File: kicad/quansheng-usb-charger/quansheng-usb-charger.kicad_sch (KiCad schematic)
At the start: 32 parts, among them J1 USB_C_Receptacle_USB2.0, U1 IP2326

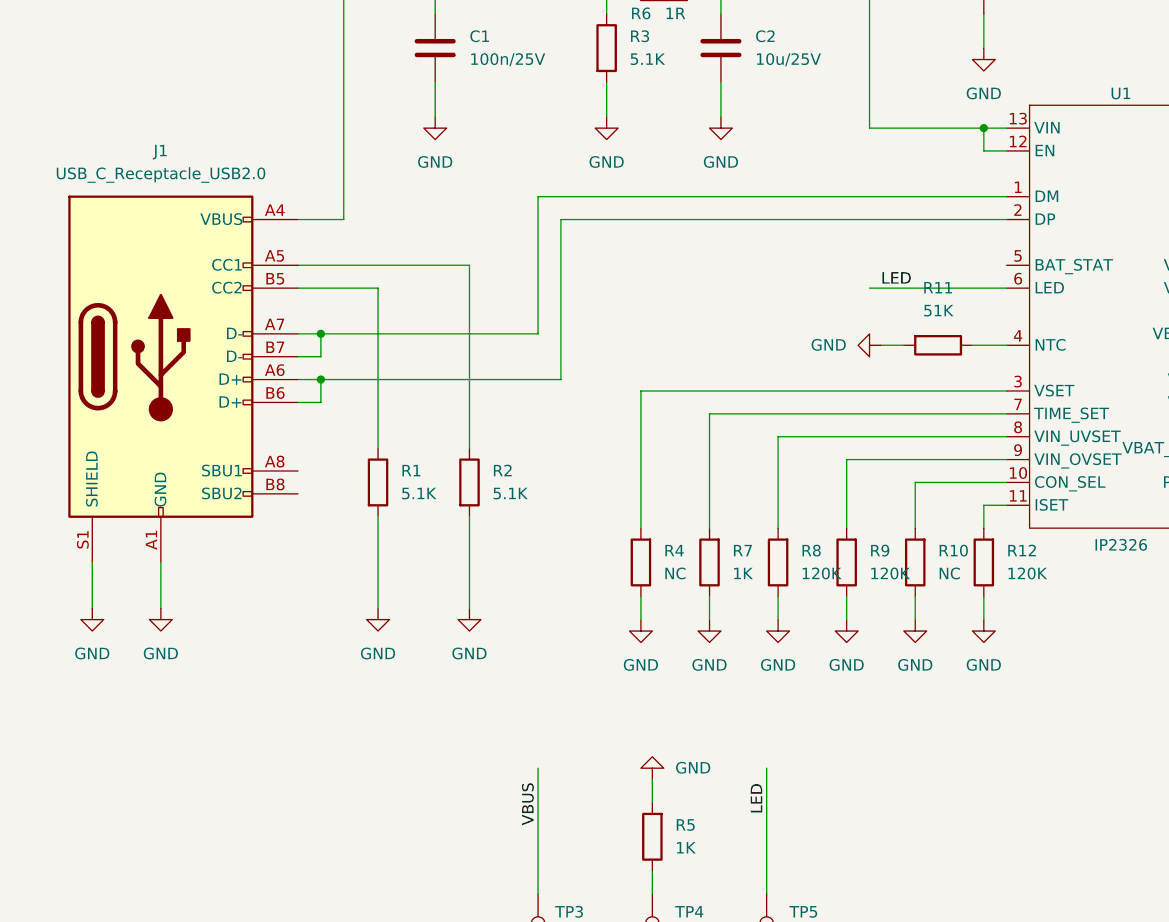
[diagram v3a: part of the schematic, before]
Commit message: Don't use the built-in USB AFC standard
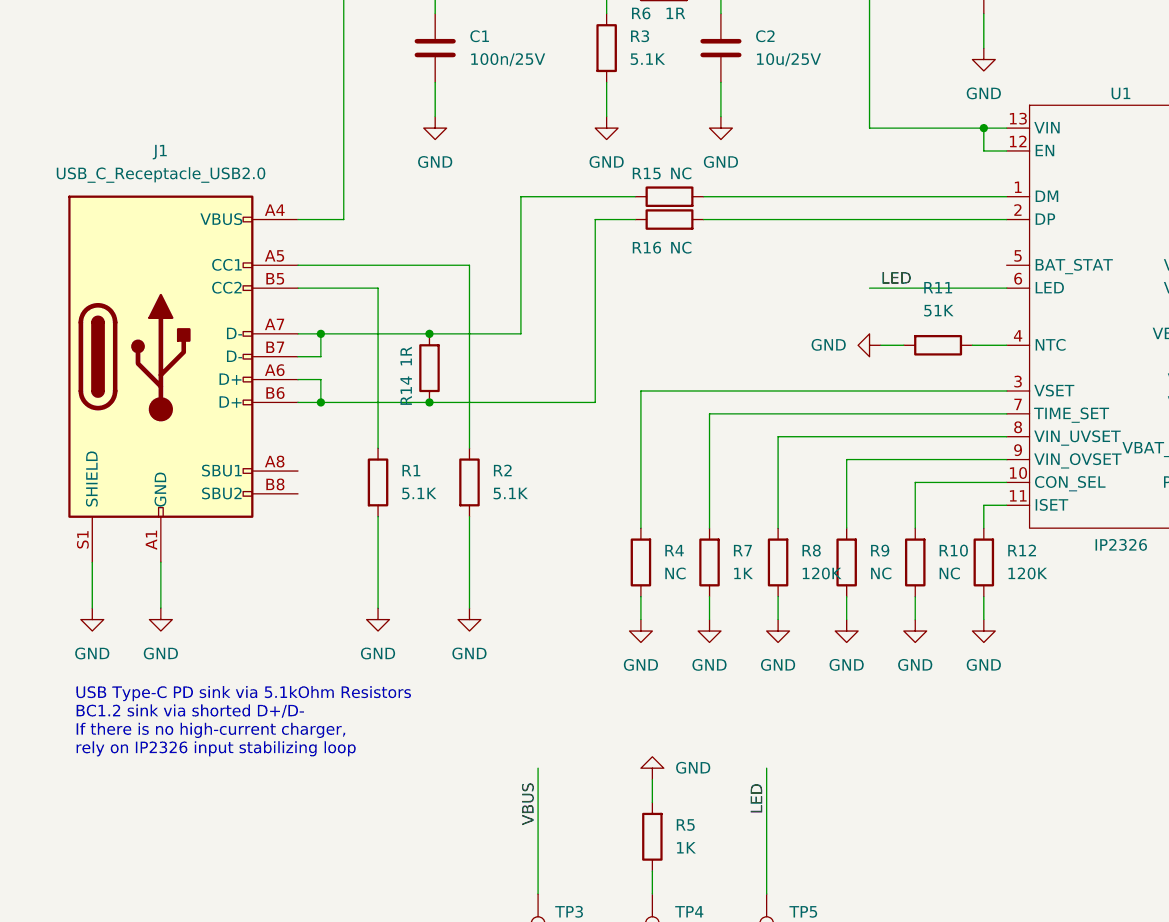
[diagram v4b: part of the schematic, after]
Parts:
- added R14: 1R, Resistor_SMD:R_0603_1608Metric, symbol Device:R
- added R15, R16: NC, Resistor_SMD:R_0603_1608Metric, symbol Device:R
- R9: value 120K -> NC; LCSC C25808 -> (none)
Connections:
- net at J1.A6 (D+), J1.B6 (D+): now also R14.1, R16.1; no longer U1.2 (DP)
- net at J1.A7 (D-), J1.B7 (D-): now also R14.2, R15.1; no longer U1.1 (DM)
- new net: R15.2, U1.1 (DM)
- new net: R16.2, U1.2 (DP)
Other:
- note added: "USB Type-C PD sink via 5.1kOhm Resistors BC1.2 sink via shorted D+/D- If there is no high-current charger, rely on IP2326 input stabilizing loop"
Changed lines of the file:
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@@
   (junction (at 177.8 99.06) (diameter 0) (color 0 0 0 0)
   )
+  (junction (at 75.565 99.06) (diameter 0) (color 0 0 0 0)
+  )
   (junction (at 171.45 68.58) (diameter 0) (color 0 0 0 0)
   )
@@
   (junction (at 107.95 53.34) (diameter 0) (color 0 0 0 0)
   )
+  (junction (at 63.5 99.06) (diameter 0) (color 0 0 0 0)
+  )
   (junction (at 95.25 53.34) (diameter 0) (color 0 0 0 0)
   )
-  (junction (at 63.5 96.52) (diameter 0) (color 0 0 0 0)
-  )
   (junction (at 137.16 44.45) (diameter 0) (color 0 0 0 0)
   )
@@
   (junction (at 95.25 50.165) (diameter 0) (color 0 0 0 0)
   )
+  (junction (at 75.565 91.44) (diameter 0) (color 0 0 0 0)
+  )
   (junction (at 95.25 44.45) (diameter 0) (color 0 0 0 0)
   )
@@
     (stroke (width 0) (type default) (color 0 0 0 0))
   )
+  (wire (pts (xy 75.565 99.06) (xy 93.98 99.06))
+    (stroke (width 0) (type default) (color 0 0 0 0))
+  )
+  (wire (pts (xy 98.425 78.74) (xy 93.98 78.74))
+    (stroke (width 0) (type default) (color 0 0 0 0))
+  )
   (wire (pts (xy 125.73 92.71) (xy 128.27 92.71))
     (stroke (width 0) (type default) (color 0 0 0 0))
@@
     (stroke (width 0) (type default) (color 0 0 0 0))
   )
-  (wire (pts (xy 63.5 91.44) (xy 87.63 91.44))
+  (wire (pts (xy 63.5 91.44) (xy 75.565 91.44))
     (stroke (width 0) (type default) (color 0 0 0 0))
   )
@@
     (stroke (width 0) (type default) (color 0 0 0 0))
   )
-  (wire (pts (xy 90.17 96.52) (xy 63.5 96.52))
+  (wire (pts (xy 106.045 76.2) (xy 139.7 76.2))
+    (stroke (width 0) (type default) (color 0 0 0 0))
+  )
+  (wire (pts (xy 93.98 78.74) (xy 93.98 99.06))
     (stroke (width 0) (type default) (color 0 0 0 0))
   )
@@
     (stroke (width 0) (type default) (color 0 0 0 0))
   )
+  (wire (pts (xy 106.045 78.74) (xy 139.7 78.74))
+    (stroke (width 0) (type default) (color 0 0 0 0))
+  )
+  (wire (pts (xy 85.725 76.2) (xy 98.425 76.2))
+    (stroke (width 0) (type default) (color 0 0 0 0))
+  )
+  (wire (pts (xy 75.565 91.44) (xy 85.725 91.44))
+    (stroke (width 0) (type default) (color 0 0 0 0))
+  )
   (wire (pts (xy 121.92 113.03) (xy 121.92 105.41))
     (stroke (width 0) (type default) (color 0 0 0 0))
@@
     (stroke (width 0) (type default) (color 0 0 0 0))
   )
-  (wire (pts (xy 87.63 91.44) (xy 87.63 76.2))
+  (wire (pts (xy 85.725 91.44) (xy 85.725 76.2))
     (stroke (width 0) (type default) (color 0 0 0 0))
   )
@@
     (stroke (width 0) (type default) (color 0 0 0 0))
   )
-  (wire (pts (xy 139.7 78.74) (xy 90.17 78.74))
-    (stroke (width 0) (type default) (color 0 0 0 0))
-  )
   (wire (pts (xy 135.89 92.71) (xy 139.7 92.71))
     (stroke (width 0) (type default) (color 0 0 0 0))
@@
     (stroke (width 0) (type default) (color 0 0 0 0))
   )
-  (wire (pts (xy 87.63 76.2) (xy 139.7 76.2))
-    (stroke (width 0) (type default) (color 0 0 0 0))
-  )
   (wire (pts (xy 121.92 105.41) (xy 139.7 105.41))
     (stroke (width 0) (type default) (color 0 0 0 0))
@@
     (stroke (width 0) (type default) (color 0 0 0 0))
   )
+  (wire (pts (xy 63.5 99.06) (xy 75.565 99.06))
+    (stroke (width 0) (type default) (color 0 0 0 0))
+  )
   (wire (pts (xy 203.2 63.5) (xy 207.01 63.5))
     (stroke (width 0) (type default) (color 0 0 0 0))
@@
     (stroke (width 0) (type default) (color 0 0 0 0))
   )
-  (wire (pts (xy 90.17 78.74) (xy 90.17 96.52))
-    (stroke (width 0) (type default) (color 0 0 0 0))
-  )
   (wire (pts (xy 165.1 86.36) (xy 167.64 86.36))
     (stroke (width 0) (type default) (color 0 0 0 0))
@@
   (wire (pts (xy 99.06 120.65) (xy 99.06 123.19))
     (stroke (width 0) (type default) (color 0 0 0 0))
+  )
+  (text "USB Type-C PD sink via 5.1kOhm Resistors\nBC1.2 sink via shorted D+/D-\nIf there is no high-current charger, \nrely on IP2326 input stabilizing loop"
+    (at 36.195 138.43 0)
+    (effects (font (size 1.27 1.27)) (justify left bottom))
   )
   (label "VBUS" (at 87.63 146.05 90)
@@
       (effects (font (size 1.27 1.27)) (justify right))
     )
-    (property "Value" "120K" (id 1) (at 124.46 118.1099 0)
+    (property "Value" "NC" (id 1) (at 124.46 118.1099 0)
       (effects (font (size 1.27 1.27)) (justify right))
     )
@@
       (effects (font (size 1.27 1.27)) hide)
     )
-    (property "LCSC" "C25808" (id 4) (at 124.46 115.5699 0)
+    (property "LCSC" "" (id 4) (at 124.46 115.5699 0)
       (effects (font (size 1.27 1.27)) hide)
     )
@@
     )
     (property "LCSC" "C21190" (id 4) (at 102.87 146.0499 0)
+      (effects (font (size 1.27 1.27)) hide)
+    )
+    (pin "1")
+    (pin "2")
+  )
+  (symbol (lib_id "Device:R") (at 102.235 76.2 90) (unit 1)
+    (in_bom yes) (on_board yes)
+    (property "Reference" "R15" (id 0) (at 99.695 73.66 90))
+    (property "Value" "NC" (id 1) (at 103.505 73.66 90))
+    (property "Footprint" "Resistor_SMD:R_0603_1608Metric" (id 2) (at 102.235 77.978 90)
+      (effects (font (size 1.27 1.27)) hide)
+    )
+    (property "Datasheet" "~" (id 3) (at 102.235 76.2 0)
+      (effects (font (size 1.27 1.27)) hide)
+    )
+    (property "LCSC" "" (id 4) (at 99.695 73.66 0)
       (effects (font (size 1.27 1.27)) hide)
     )
@@
     )
     (pin "1")
+  )
+  (symbol (lib_id "Device:R") (at 75.565 95.25 180) (unit 1)
+    (in_bom yes) (on_board yes)
+    (property "Reference" "R14" (id 0) (at 73.025 97.79 90))
+    (property "Value" "1R" (id 1) (at 73.025 93.98 90))
+    (property "Footprint" "Resistor_SMD:R_0603_1608Metric" (id 2) (at 77.343 95.25 90)
+      (effects (font (size 1.27 1.27)) hide)
+    )
+    (property "Datasheet" "~" (id 3) (at 75.565 95.25 0)
+      (effects (font (size 1.27 1.27)) hide)
+    )
+    (property "LCSC" "C22936" (id 4) (at 73.025 97.79 0)
+      (effects (font (size 1.27 1.27)) hide)
+    )
+    (pin "1")
+    (pin "2")
   )
   (symbol (lib_id "Device:R") (at 101.6 50.165 90) (unit 1)
@@
     (pin "2")
   )
+  (symbol (lib_id "Device:R") (at 102.235 78.74 90) (unit 1)
+    (in_bom yes) (on_board yes)
+    (property "Reference" "R16" (id 0) (at 99.695 81.915 90))
+    (property "Value" "NC" (id 1) (at 103.505 81.915 90))
+    (property "Footprint" "Resistor_SMD:R_0603_1608Metric" (id 2) (at 102.235 80.518 90)
+      (effects (font (size 1.27 1.27)) hide)
+    )
+    (property "Datasheet" "~" (id 3) (at 102.235 78.74 0)
+      (effects (font (size 1.27 1.27)) hide)
+    )
+    (property "LCSC" "" (id 4) (at 99.695 76.2 0)
+      (effects (font (size 1.27 1.27)) hide)
+    )
+    (pin "1")
+    (pin "2")
+  )
   (symbol (lib_id "Device:L") (at 151.13 44.45 90) (unit 1)
     (in_bom yes) (on_board yes) (fields_autoplaced)
@@
     )
     (path "/10118daf-f47d-4d24-8bea-5685faf34786"
-      (reference "R9") (unit 1) (value "120K") (footprint "Resistor_SMD:R_0603_1608Metric")
+      (reference "R9") (unit 1) (value "NC") (footprint "Resistor_SMD:R_0603_1608Metric")
     )
     (path "/63df9b76-090c-4e7a-baea-2d93ffcedf98"
@@
       (reference "R13") (unit 1) (value "1R") (footprint "Resistor_SMD:R_0603_1608Metric")
     )
+    (path "/880c680a-7e6c-48f7-8226-9c3889b584d9"
+      (reference "R14") (unit 1) (value "1R") (footprint "Resistor_SMD:R_0603_1608Metric")
+    )
+    (path "/1eae0866-fb43-460e-ba70-4206816f3ae0"
+      (reference "R15") (unit 1) (value "NC") (footprint "Resistor_SMD:R_0603_1608Metric")
+    )
+    (path "/af3a5ad9-3c72-4849-ad9e-dec0a7570455"
+      (reference "R16") (unit 1) (value "NC") (footprint "Resistor_SMD:R_0603_1608Metric")
+    )
     (path "/9b3c58a7-a9b9-4498-abc0-f9f43e4f0292"

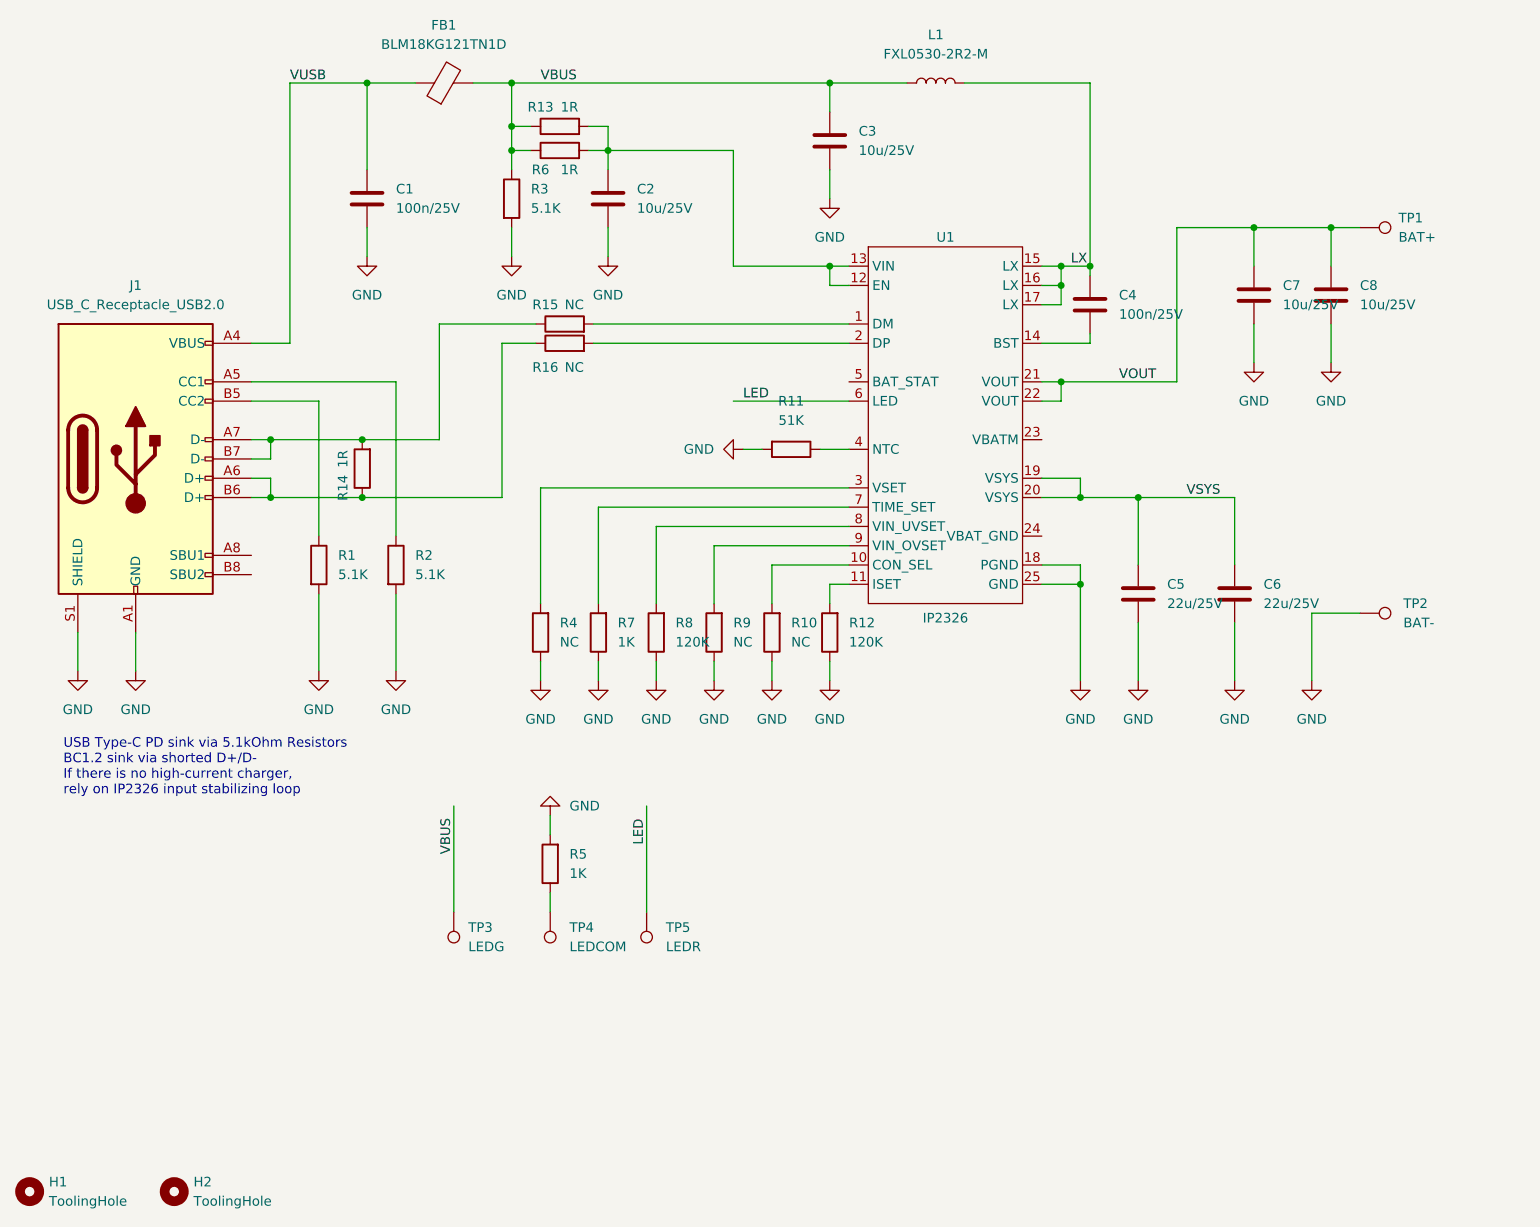
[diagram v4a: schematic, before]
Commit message: Add jumper pad for optional 1.5A charging current
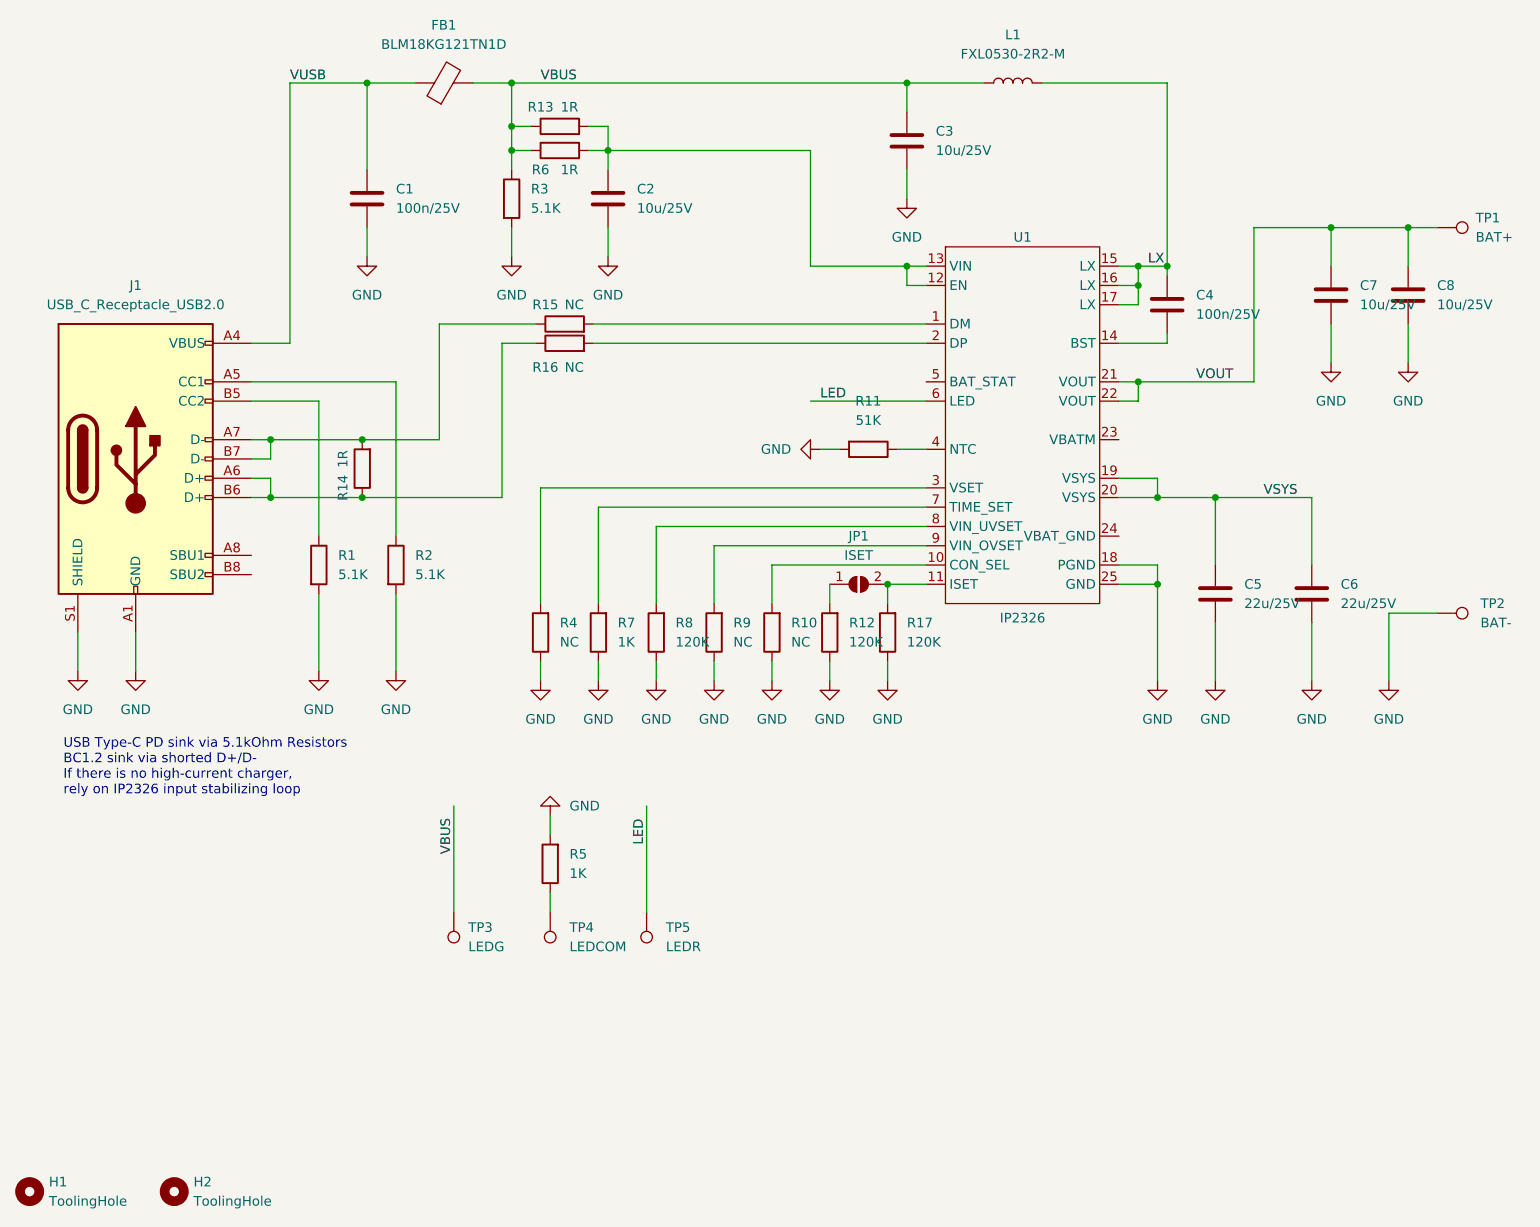
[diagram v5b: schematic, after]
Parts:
- added JP1: ISET, Jumper:SolderJumper-2_P1.3mm_Open_TrianglePad1.0x1.5mm, symbol Jumper:SolderJumper_2_Open
- added R17: 120K, Resistor_SMD:R_0603_1608Metric, symbol Device:R
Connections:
- net GND: now also R17.1
- net at U1.11 (ISET): now also JP1.2 (B), R17.2; no longer R12.2
- new net: JP1.1 (A), R12.2
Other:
- moved on the sheet: C3, C4, C5, C6, C7, C8, L1, R11, TP1, TP2, U1
